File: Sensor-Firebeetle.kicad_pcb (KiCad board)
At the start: 2 copper layers, 41.3 x 104.7 mm, 13 parts, among them J1 Solar Panel, J2 Battery, SW1 Sensor Number, U1 DFR0654, U2 BME280, U3 TP4056

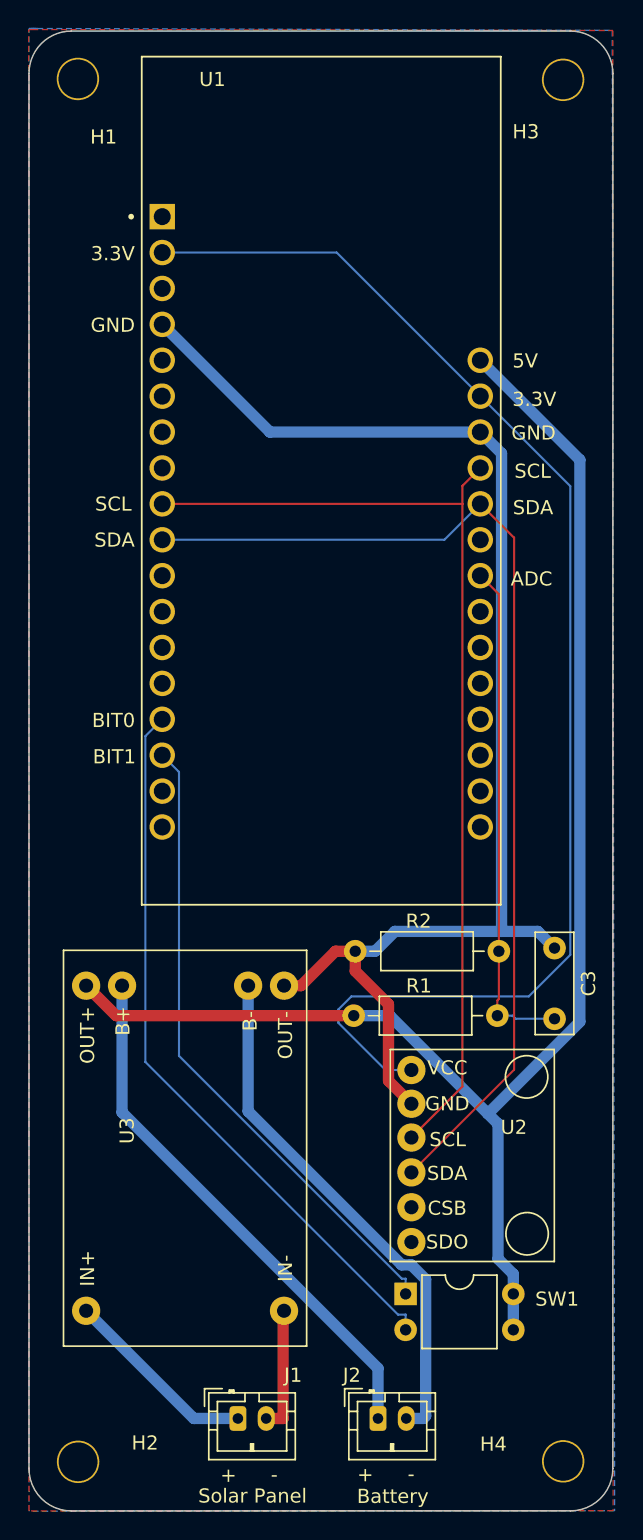
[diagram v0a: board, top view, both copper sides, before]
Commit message: 3.3V for switches
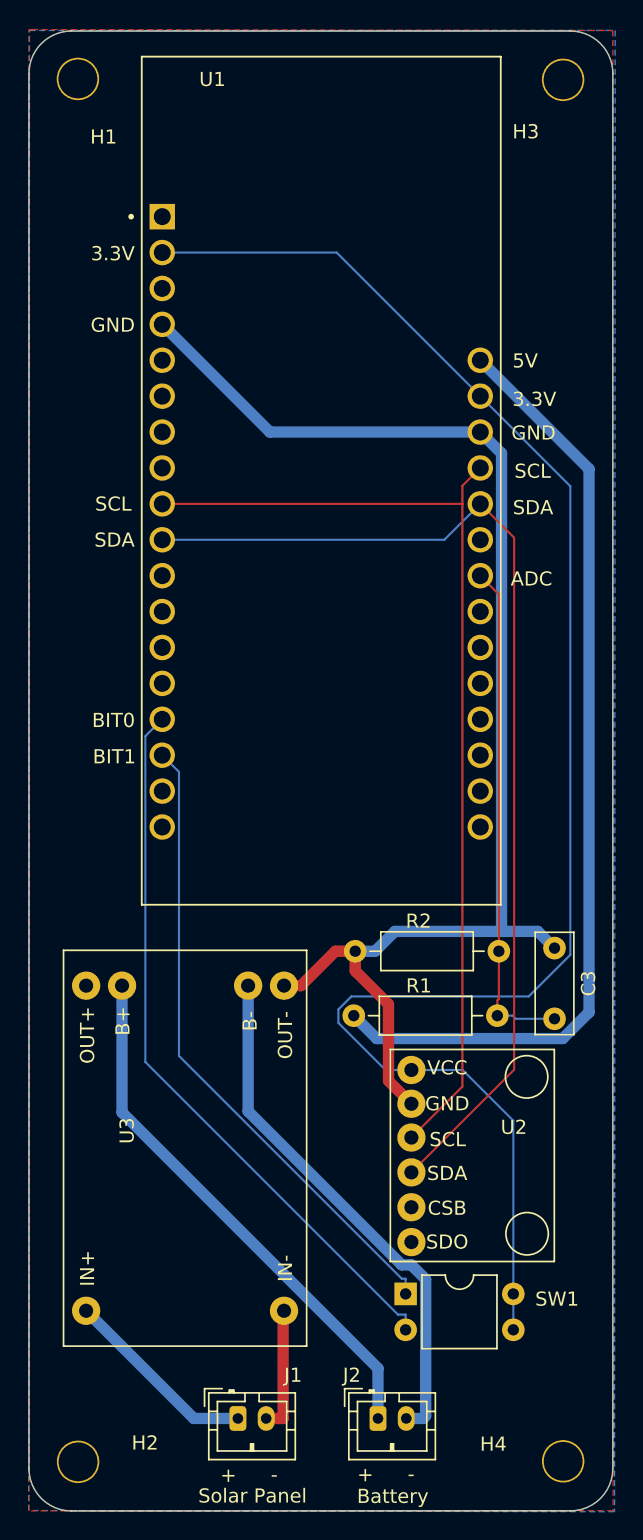
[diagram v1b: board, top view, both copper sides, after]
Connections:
- SW1 pad 3: +5V -> +3.3V
- SW1 pad 4: +5V -> +3.3V
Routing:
- net +5V: track 107.1 -> 67.4 mm
- net +3.3V: track 94.4 -> 117.9 mm
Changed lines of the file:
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@@
       (net 13 "Bit1") (pintype "passive"))
     (pad "3" thru_hole oval (at 7.62 2.54) (size 1.6 1.6) (drill 0.8) (layers *.Cu *.Mask)
-      (net 1 "+5V") (pintype "passive"))
+      (net 27 "+3.3V") (pintype "passive"))
     (pad "4" thru_hole oval (at 7.62 0) (size 1.6 1.6) (drill 0.8) (layers *.Cu *.Mask)
-      (net 1 "+5V") (pintype "passive"))
+      (net 27 "+3.3V") (pintype "passive"))
     (model "${KICAD6_3DMODEL_DIR}/Package_DIP.3dshapes/DIP-4_W7.62mm.wrl"
       (offset (xyz 0 0 0))
@@
     (effects (font (size 1 1) (thickness 0.25)))
   )
-  (segment (start 101.3126 130.4733) (end 84.5034 130.4733) (width 0.8) (layer "F.Cu") (net 1))
-  (segment (start 84.5034 130.4733) (end 82.3808 128.3507) (width 0.8) (layer "F.Cu") (net 1))
-  (segment (start 111.5208 138.1262) (end 111.5208 147.6762) (width 0.8) (layer "B.Cu") (net 1))
-  (segment (start 112.6025 150.1582) (end 112.6025 152.6982) (width 0.8) (layer "B.Cu") (net 1))
-  (segment (start 110.8034 137.4087) (end 117.3091 130.903) (width 0.8) (layer "B.Cu") (net 1))
-  (segment (start 117.3091 91.1507) (end 110.2646 84.1062) (width 0.8) (layer "B.Cu") (net 1))
-  (segment (start 101.3126 130.4733) (end 103.8679 130.4733) (width 0.8) (layer "B.Cu") (net 1))
-  (segment (start 111.5208 147.6762) (end 112.6025 148.7579) (width 0.8) (layer "B.Cu") (net 1))
-  (segment (start 103.8679 130.4733) (end 110.8034 137.4087) (width 0.8) (layer "B.Cu") (net 1))
-  (segment (start 112.6025 150.1582) (end 112.6025 148.7579) (width 0.8) (layer "B.Cu") (net 1))
-  (segment (start 117.3091 130.903) (end 117.3091 91.1507) (width 0.8) (layer "B.Cu") (net 1))
-  (segment (start 110.8034 137.4087) (end 111.5208 138.1262) (width 0.8) (layer "B.Cu") (net 1))
+  (segment (start 110.2646 84.1062) (end 117.957077 91.798677) (width 0.8) (layer "B.Cu") (net 1))
+  (segment (start 117.957077 130.233522) (end 116.096699 132.0939) (width 0.8) (layer "B.Cu") (net 1))
+  (segment (start 102.9332 132.0939) (end 101.3126 130.4733) (width 0.8) (layer "B.Cu") (net 1))
+  (segment (start 116.096699 132.0939) (end 102.9332 132.0939) (width 0.8) (layer "B.Cu") (net 1))
+  (segment (start 117.957077 91.798677) (end 117.957077 130.233522) (width 0.8) (layer "B.Cu") (net 1))
   (segment (start 101.4178 125.9155) (end 101.4178 127.3158) (width 0.8) (layer "F.Cu") (net 2))
   (segment (start 105.3919 136.706) (end 103.7711 135.0852) (width 0.8) (layer "F.Cu") (net 2))
@@
   (segment (start 101.1453 129.112) (end 113.6945 129.112) (width 0.15) (layer "B.Cu") (net 27))
   (segment (start 105.3919 134.3171) (end 103.559 134.3171) (width 0.15) (layer "B.Cu") (net 27))
+  (segment (start 109.013283 134.317104) (end 112.6025 137.906321) (width 0.15) (layer "B.Cu") (net 27))
   (segment (start 103.559 134.3171) (end 100.2268 130.9849) (width 0.15) (layer "B.Cu") (net 27))
   (segment (start 116.6337 93.0153) (end 110.2646 86.6462) (width 0.15) (layer "B.Cu") (net 27))
   (segment (start 113.6945 129.112) (end 116.6337 126.1728) (width 0.15) (layer "B.Cu") (net 27))
+  (segment (start 112.6025 137.906321) (end 112.6025 150.1582) (width 0.15) (layer "B.Cu") (net 27))
+  (segment (start 105.391893 134.317104) (end 109.013283 134.317104) (width 0.15) (layer "B.Cu") (net 27))
   (segment (start 100.2268 130.0305) (end 101.1453 129.112) (width 0.15) (layer "B.Cu") (net 27))
   (segment (start 100.2268 130.9849) (end 100.2268 130.0305) (width 0.15) (layer "B.Cu") (net 27))
   (segment (start 116.6337 126.1728) (end 116.6337 93.0153) (width 0.15) (layer "B.Cu") (net 27))
+  (segment (start 112.6025 150.1582) (end 112.6025 152.6982) (width 0.15) (layer "B.Cu") (net 27))
   (segment (start 110.2646 86.6462) (end 100.1046 76.4862) (width 0.15) (layer "B.Cu") (net 27))
   (segment (start 100.1046 76.4862) (end 87.7646 76.4862) (width 0.15) (layer "B.Cu") (net 27))
@@
     (polygon
       (pts
-        (xy 78.91534 60.635349)
-        (xy 119.598239 60.768877)
-        (xy 119.767505 165.495764)
-        (xy 78.344085 165.532957)
-        (xy 78.336064 60.631451)
-        (xy 78.693171 60.619137)
+        (xy 119.761395 165.567668)
+        (xy 78.32929 165.486667)
+        (xy 78.37054 60.779886)
+        (xy 78.376472 60.772389)
+        (xy 119.808577 60.772389)
       )
     )
